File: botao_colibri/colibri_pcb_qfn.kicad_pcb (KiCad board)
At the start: 2 copper layers, 72.5 x 47.1 mm, 39 parts, among them J1 USB4970-00-A_REVA, J2 TC2030, J3 Conn_01x02, J4 PJ-307C, SW1 B3F-3122, U1 ME54BS12, U4 NPM1300-QEAA-R7

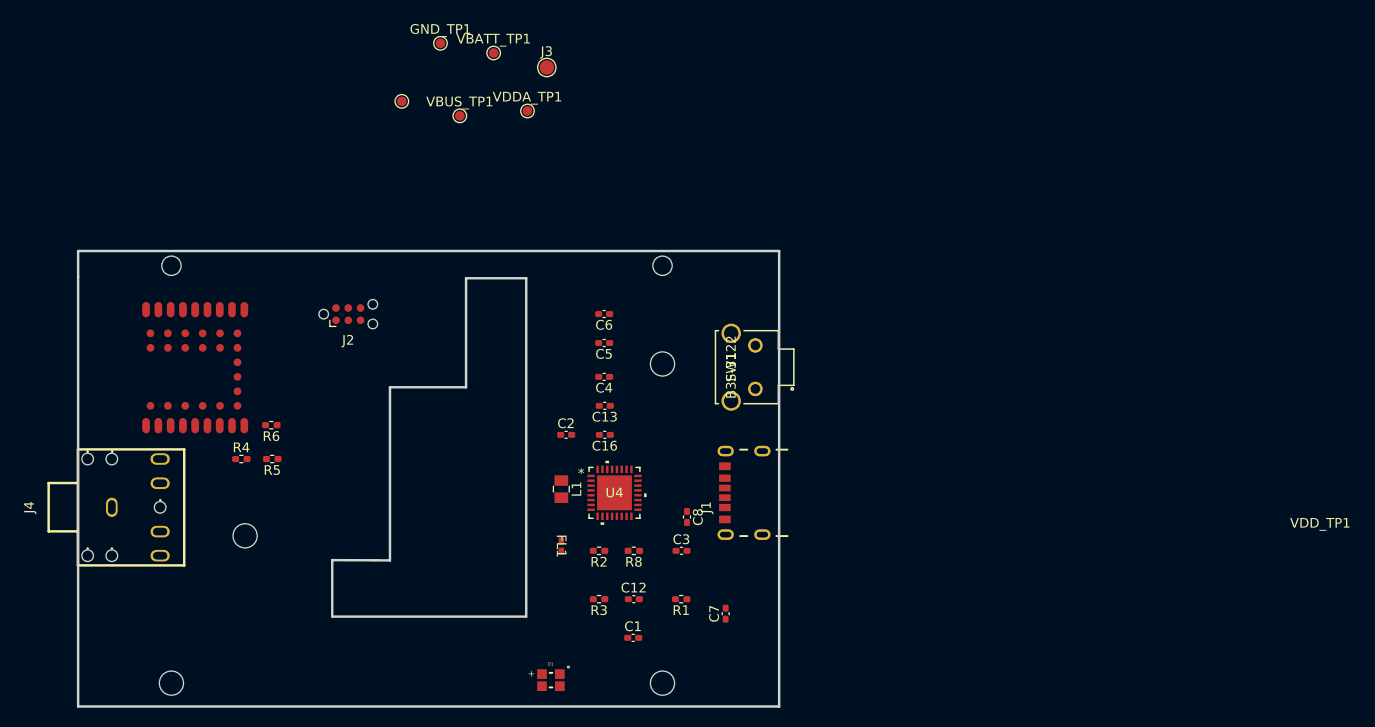
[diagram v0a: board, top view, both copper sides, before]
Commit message: mudanças de posição de componentes
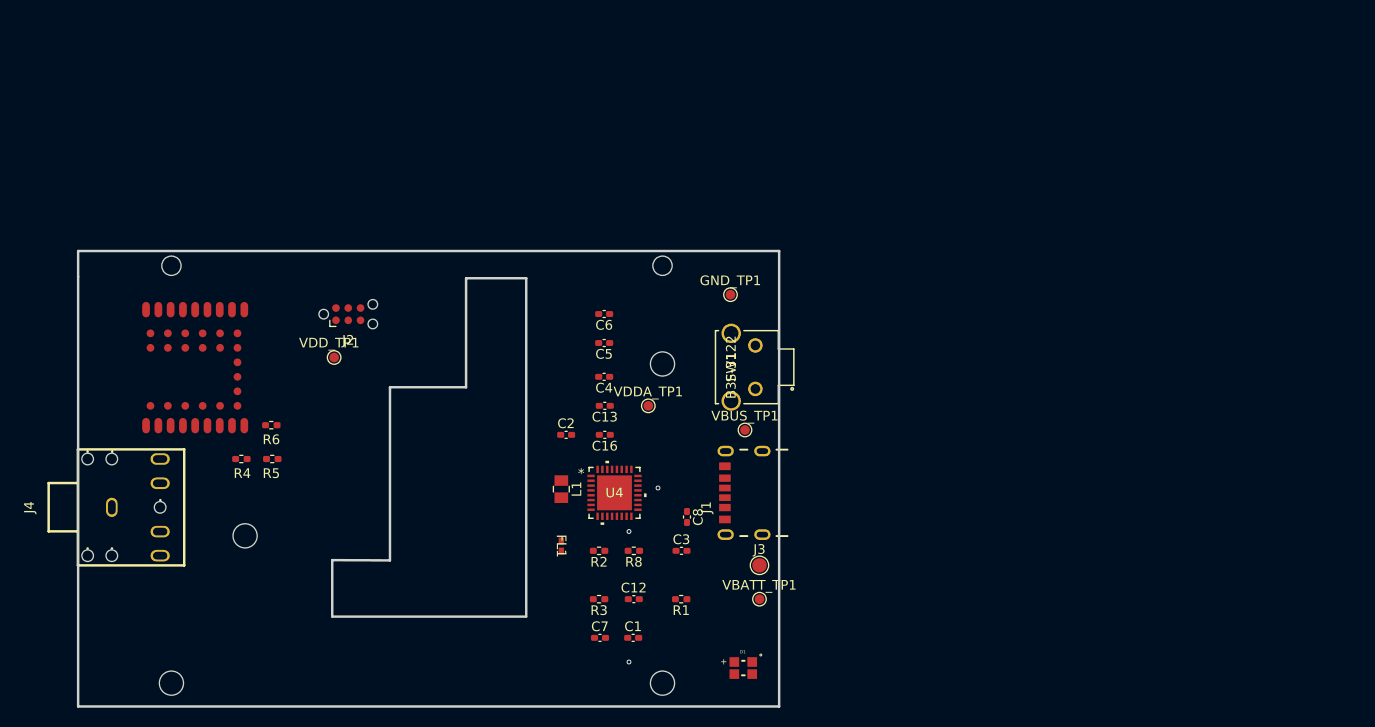
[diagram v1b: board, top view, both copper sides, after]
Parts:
- moved VBATT_TP1 62.8 mm to (194.5, 108.5)
- moved J3 56.0 mm to (194.5, 105.0)
- moved VBUS_TP1 43.9 mm to (193.0, 91.0)
- moved GND_TP1 39.7 mm to (191.5, 77.0)
- moved VDDA_TP1 33.0 mm to (183.0, 88.5)
- moved VDD_TP1 27.4 mm to (150.5, 83.5)
- moved D1 19.9 mm to (192.8, 115.6)
- moved C7 13.2 mm to (178.0, 112.5), turned to 0 degrees
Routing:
- net (no net): vias 0 -> 3
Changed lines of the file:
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@@
 	(footprint "colibri-v4:WL-SFCD_0805"
 		(layer "F.Cu")
-		(at 172.925 116.875)
+		(at 192.825 115.625)
 		(property "Reference" "D1"
 			(at -0.04 -1.6732 0)
@@
 	(footprint "TestPoint:TestPoint_Pad_D1.5mm"
 		(layer "F.Cu")
-		(at 172.5 53.5)
+		(at 194.5 105)
 		(descr "SMD pad as test Point, diameter 1.5mm")
 		(tags "test point SMD pad")
@@
 		(tags "resistor handsolder")
 		(property "Reference" "R4"
-			(at 0 -1.17 0)
+			(at 0.0975 1.5 0)
 			(layer "F.SilkS")
 			(effects
@@
 		(tags "resistor handsolder")
 		(property "Reference" "R6"
-			(at 0 -1.17 0)
+			(at 0 -1.5 0)
 			(layer "F.SilkS")
 			(effects
@@
 	(footprint "TestPoint:TestPoint_Pad_D1.0mm"
 		(layer "F.Cu")
-		(at 161.5 51)
+		(at 191.5 77)
 		(descr "SMD pad as test Point, diameter 1.0mm")
 		(tags "test point SMD pad")
@@
 	(footprint "Capacitor_SMD:C_0402_1005Metric_Pad0.74x0.62mm_HandSolder"
 		(layer "F.Cu")
-		(at 191 110 90)
+		(at 178 112.5)
 		(descr "Capacitor SMD 0402 (1005 Metric), square (rectangular) end terminal, IPC-7351 nominal with elongated pad for handsoldering. (Body size source: IPC-SM-782 page 76, https://www.pcb-3d.com/wordpress/wp-content/uploads/ipc-sm-782a_amendment_1_and_2.pdf)")
 		(tags "capacitor handsolder")
 		(property "Reference" "C7"
-			(at 0 -1.16 90)
+			(at 0 -1.16 0)
 			(layer "F.SilkS")
 			(effects
@@
 		)
 		(property "Value" "C_Small"
-			(at 0 1.16 90)
+			(at 0 1.16 0)
 			(layer "F.Fab")
 			(effects
@@
 		)
 		(property "Datasheet" ""
-			(at 0 0 90)
+			(at 0 0 0)
 			(layer "F.Fab")
 			(hide yes)
@@
 		)
 		(property "Description" "Unpolarized capacitor, small symbol"
-			(at 0 0 90)
+			(at 0 0 0)
 			(layer "F.Fab")
 			(hide yes)
@@
 		)
 		(property "KiLib_Generator" "SMD_2terminal_chip_molded"
-			(at 0 0 90)
+			(at 0 0 0)
 			(layer "F.SilkS")
 			(hide yes)
@@
 		)
 		(fp_text user "${REFERENCE}"
-			(at 0 0 90)
+			(at 0 0 0)
 			(layer "F.Fab")
 			(effects
@@
 		)
 		(pad "1" smd roundrect
-			(at -0.5675 0 90)
+			(at -0.5675 0)
 			(size 0.735 0.62)
 			(layers "F.Cu" "F.Mask" "F.Paste")
@@
 		)
 		(pad "2" smd roundrect
-			(at 0.5675 0 90)
+			(at 0.5675 0)
 			(size 0.735 0.62)
 			(layers "F.Cu" "F.Mask" "F.Paste")
@@
 	(footprint "TestPoint:TestPoint_Pad_D1.0mm"
 		(layer "F.Cu")
-		(at 167 52)
+		(at 194.5 108.5)
 		(descr "SMD pad as test Point, diameter 1.0mm")
 		(tags "test point SMD pad")
@@
 	(footprint "TestPoint:TestPoint_Pad_D1.0mm"
 		(layer "F.Cu")
-		(at 170.5 58)
+		(at 183 88.5)
 		(descr "SMD pad as test Point, diameter 1.0mm")
 		(tags "test point SMD pad")
@@
 	(footprint "TestPoint:TestPoint_Pad_D1.0mm"
 		(layer "F.Cu")
-		(at 163.5 58.5)
+		(at 193 91)
 		(descr "SMD pad as test Point, diameter 1.0mm")
 		(tags "test point SMD pad")
@@
 	(footprint "TestPoint:TestPoint_Pad_D1.0mm"
 		(layer "F.Cu")
-		(at 157.5 57)
+		(at 150.5 83.5)
 		(descr "SMD pad as test Point, diameter 1.0mm")
 		(tags "test point SMD pad")
 		(property "Reference" "VDD_TP1"
-			(at 95.0175 43.637 0)
+			(at -0.5 -1.5 0)
 			(layer "F.SilkS")
 			(effects
@@
 		)
 		(fp_text user "${REFERENCE}"
-			(at 95.0175 43.635 0)
+			(at -0.5 -1.502 0)
 			(layer "F.Fab")
 			(effects
@@
 		(tags "resistor handsolder")
 		(property "Reference" "R5"
-			(at 0 -1.17 0)
+			(at 0.0975 -1.5 0)
 			(layer "F.SilkS")
 			(effects
@@
 		(net "")
 	)
+	(via
+		(at 184 97)
+		(size 0.5)
+		(drill 0.3)
+		(layers "F.Cu" "B.Cu")
+		(net "")
+	)
+	(via
+		(at 181 101.5)
+		(size 0.5)
+		(drill 0.3)
+		(layers "F.Cu" "B.Cu")
+		(net "")
+	)
+	(via
+		(at 181 115)
+		(size 0.5)
+		(drill 0.3)
+		(layers "F.Cu" "B.Cu")
+		(net "")
+	)

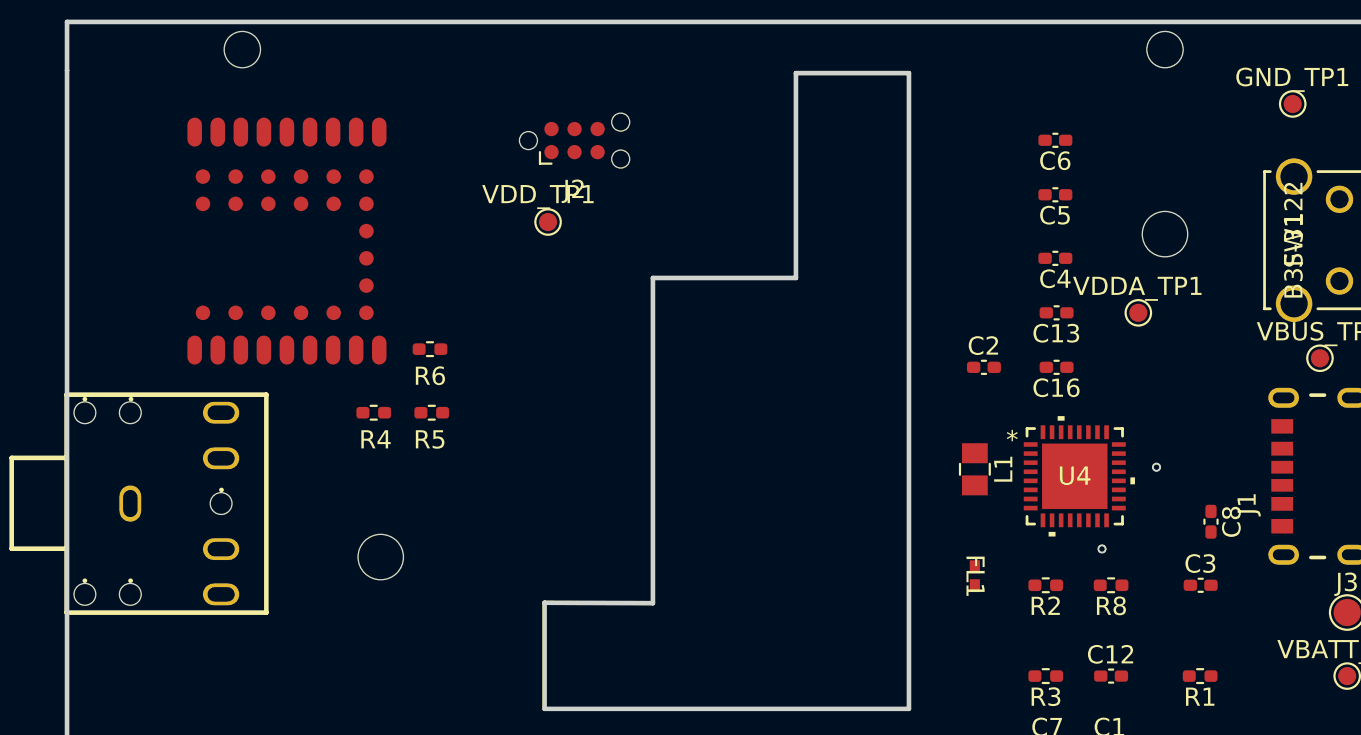
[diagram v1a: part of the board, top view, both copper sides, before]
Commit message: Desenho do silk do microcontrolador
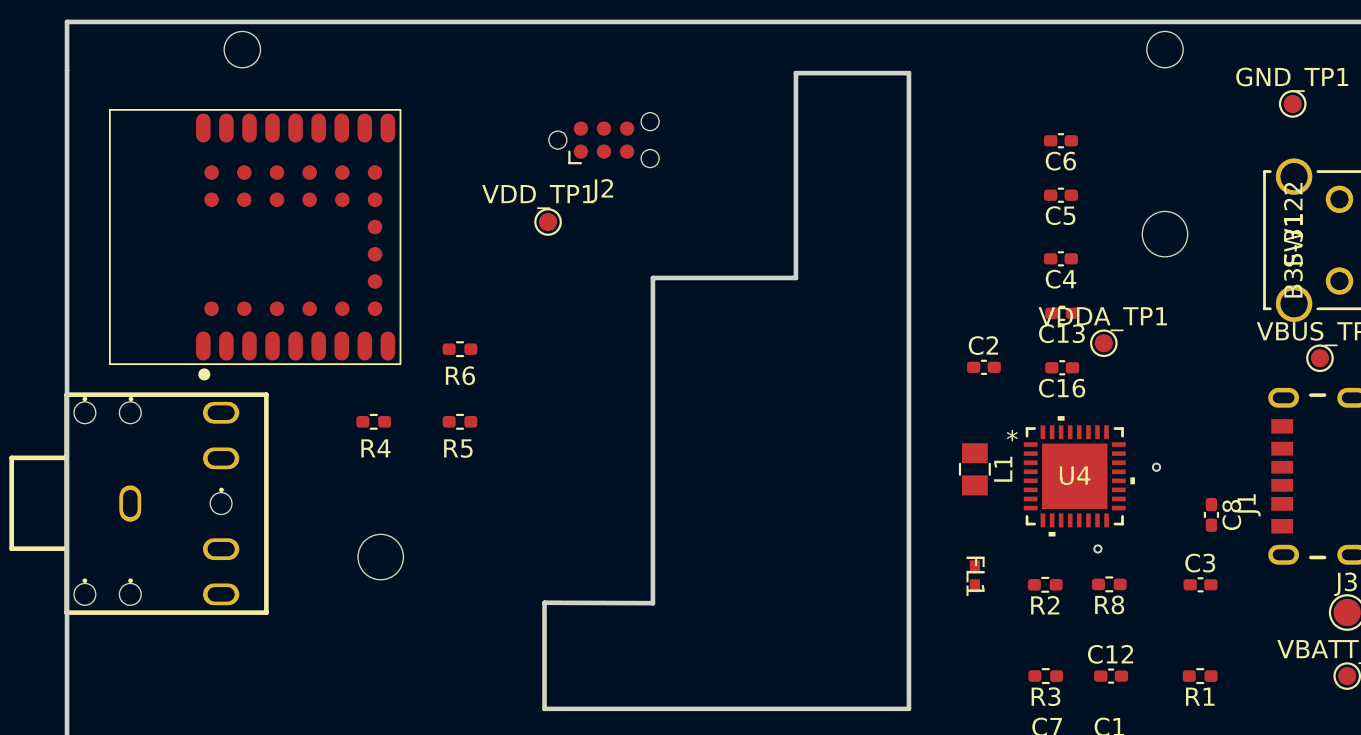
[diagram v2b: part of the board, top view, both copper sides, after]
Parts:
- moved VDDA_TP1 2.53 mm to (181.1, 90.2)
- moved R6 1.65 mm to (145.7, 90.5)
- moved R5 1.63 mm to (145.7, 94.5)
- moved J2 1.62 mm to (153.6, 79.0)
- moved U1 0.53 mm to (142.4, 90.3)
- moved R4 0.50 mm to (140.9, 94.5)
- moved C8 0.38 mm to (187.0, 99.6)
- moved C13 0.31 mm to (178.8, 88.5)
- moved C16 0.31 mm to (178.8, 91.5)
- moved C4 0.31 mm to (178.7, 85.5)
- moved C5 0.31 mm to (178.7, 82.0)
- moved C6 0.31 mm to (178.7, 79.0)
- moved R8 0.11 mm to (181.4, 103.5)
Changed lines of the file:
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@@
 	(footprint "Capacitor_SMD:C_0402_1005Metric_Pad0.74x0.62mm_HandSolder"
 		(layer "F.Cu")
-		(at 178.4325 79 180)
+		(at 178.74 79.025 180)
 		(descr "Capacitor SMD 0402 (1005 Metric), square (rectangular) end terminal, IPC-7351 nominal with elongated pad for handsoldering. (Body size source: IPC-SM-782 page 76, https://www.pcb-3d.com/wordpress/wp-content/uploads/ipc-sm-782a_amendment_1_and_2.pdf)")
 		(tags "capacitor handsolder")
@@
 	(footprint "Connector:Tag-Connect_TC2030-IDC-NL_2x03_P1.27mm_Vertical"
 		(layer "F.Cu")
-		(at 151.96 79.016)
+		(at 153.58 78.99)
 		(descr "Tag-Connect programming header; http://www.tag-connect.com/Materials/TC2030-IDC-NL.pdf")
 		(tags "tag connect programming header pogo pins")
@@
 			(polygon
 				(pts
-					(xy 153.23 78.381) (xy 150.69 78.381) (xy 150.69 79.651) (xy 153.23 79.651)
+					(xy 154.85 78.355) (xy 152.31 78.355) (xy 152.31 79.625) (xy 154.85 79.625)
 				)
 			)
@@
 	(footprint "Capacitor_SMD:C_0402_1005Metric_Pad0.74x0.62mm_HandSolder"
 		(layer "F.Cu")
-		(at 186.4325 103.5)
+		(at 186.425 103.475)
 		(descr "Capacitor SMD 0402 (1005 Metric), square (rectangular) end terminal, IPC-7351 nominal with elongated pad for handsoldering. (Body size source: IPC-SM-782 page 76, https://www.pcb-3d.com/wordpress/wp-content/uploads/ipc-sm-782a_amendment_1_and_2.pdf)")
 		(tags "capacitor handsolder")
@@
 	(footprint "Resistor_SMD:R_0402_1005Metric_Pad0.72x0.64mm_HandSolder"
 		(layer "F.Cu")
-		(at 140.9025 94)
+		(at 140.9025 94.5)
 		(descr "Resistor SMD 0402 (1005 Metric), square (rectangular) end terminal, IPC-7351 nominal with elongated pad for handsoldering. (Body size source: IPC-SM-782 page 72, https://www.pcb-3d.com/wordpress/wp-content/uploads/ipc-sm-782a_amendment_1_and_2.pdf)")
 		(tags "resistor handsolder")
@@
 	(footprint "Capacitor_SMD:C_0402_1005Metric_Pad0.74x0.62mm_HandSolder"
 		(layer "F.Cu")
-		(at 187 100 -90)
+		(at 187.025 99.625 -90)
 		(descr "Capacitor SMD 0402 (1005 Metric), square (rectangular) end terminal, IPC-7351 nominal with elongated pad for handsoldering. (Body size source: IPC-SM-782 page 76, https://www.pcb-3d.com/wordpress/wp-content/uploads/ipc-sm-782a_amendment_1_and_2.pdf)")
 		(tags "capacitor handsolder")
@@
 	(footprint "Resistor_SMD:R_0402_1005Metric_Pad0.72x0.64mm_HandSolder"
 		(layer "F.Cu")
-		(at 144 90.5 180)
+		(at 145.6525 90.5 180)
 		(descr "Resistor SMD 0402 (1005 Metric), square (rectangular) end terminal, IPC-7351 nominal with elongated pad for handsoldering. (Body size source: IPC-SM-782 page 72, https://www.pcb-3d.com/wordpress/wp-content/uploads/ipc-sm-782a_amendment_1_and_2.pdf)")
 		(tags "resistor handsolder")
@@
 	(footprint "Resistor_SMD:R_0402_1005Metric_Pad0.72x0.64mm_HandSolder"
 		(layer "F.Cu")
-		(at 181.5 103.5 180)
+		(at 181.4 103.45 180)
 		(descr "Resistor SMD 0402 (1005 Metric), square (rectangular) end terminal, IPC-7351 nominal with elongated pad for handsoldering. (Body size source: IPC-SM-782 page 72, https://www.pcb-3d.com/wordpress/wp-content/uploads/ipc-sm-782a_amendment_1_and_2.pdf)")
 		(tags "resistor handsolder")
@@
 	(footprint "Capacitor_SMD:C_0402_1005Metric_Pad0.74x0.62mm_HandSolder"
 		(layer "F.Cu")
-		(at 178.4325 85.5 180)
+		(at 178.74 85.525 180)
 		(descr "Capacitor SMD 0402 (1005 Metric), square (rectangular) end terminal, IPC-7351 nominal with elongated pad for handsoldering. (Body size source: IPC-SM-782 page 76, https://www.pcb-3d.com/wordpress/wp-content/uploads/ipc-sm-782a_amendment_1_and_2.pdf)")
 		(tags "capacitor handsolder")
@@
 	(footprint "Resistor_SMD:R_0402_1005Metric_Pad0.72x0.64mm_HandSolder"
 		(layer "F.Cu")
-		(at 177.9025 103.5 180)
+		(at 177.875 103.475 180)
 		(descr "Resistor SMD 0402 (1005 Metric), square (rectangular) end terminal, IPC-7351 nominal with elongated pad for handsoldering. (Body size source: IPC-SM-782 page 72, https://www.pcb-3d.com/wordpress/wp-content/uploads/ipc-sm-782a_amendment_1_and_2.pdf)")
 		(tags "resistor handsolder")
@@
 	(footprint "Capacitor_SMD:C_0402_1005Metric_Pad0.74x0.62mm_HandSolder"
 		(layer "F.Cu")
-		(at 178.4325 82 180)
+		(at 178.74 82.025 180)
 		(descr "Capacitor SMD 0402 (1005 Metric), square (rectangular) end terminal, IPC-7351 nominal with elongated pad for handsoldering. (Body size source: IPC-SM-782 page 76, https://www.pcb-3d.com/wordpress/wp-content/uploads/ipc-sm-782a_amendment_1_and_2.pdf)")
 		(tags "capacitor handsolder")
@@
 	(footprint "Capacitor_SMD:C_0402_1005Metric_Pad0.74x0.62mm_HandSolder"
 		(layer "F.Cu")
-		(at 178.5 91.5 180)
+		(at 178.8075 91.525 180)
 		(descr "Capacitor SMD 0402 (1005 Metric), square (rectangular) end terminal, IPC-7351 nominal with elongated pad for handsoldering. (Body size source: IPC-SM-782 page 76, https://www.pcb-3d.com/wordpress/wp-content/uploads/ipc-sm-782a_amendment_1_and_2.pdf)")
 		(tags "capacitor handsolder")
@@
 	(footprint "TestPoint:TestPoint_Pad_D1.0mm"
 		(layer "F.Cu")
-		(at 183 88.5)
+		(at 181.1 90.175)
 		(descr "SMD pad as test Point, diameter 1.0mm")
 		(tags "test point SMD pad")
@@
 	(footprint "Resistor_SMD:R_0402_1005Metric_Pad0.72x0.64mm_HandSolder"
 		(layer "F.Cu")
-		(at 144.0975 94 180)
+		(at 145.6525 94.5 180)
 		(descr "Resistor SMD 0402 (1005 Metric), square (rectangular) end terminal, IPC-7351 nominal with elongated pad for handsoldering. (Body size source: IPC-SM-782 page 72, https://www.pcb-3d.com/wordpress/wp-content/uploads/ipc-sm-782a_amendment_1_and_2.pdf)")
 		(tags "resistor handsolder")
@@
 	(footprint "Capacitor_SMD:C_0402_1005Metric_Pad0.74x0.62mm_HandSolder"
 		(layer "F.Cu")
-		(at 178.5 88.5 180)
+		(at 178.8075 88.525 180)
 		(descr "Capacitor SMD 0402 (1005 Metric), square (rectangular) end terminal, IPC-7351 nominal with elongated pad for handsoldering. (Body size source: IPC-SM-782 page 76, https://www.pcb-3d.com/wordpress/wp-content/uploads/ipc-sm-782a_amendment_1_and_2.pdf)")
 		(tags "capacitor handsolder")
@@
 	(footprint "colibri-v4:ME54BS12_V1.0"
 		(layer "F.Cu")
-		(at 141.9 90.55 90)
+		(at 142.375 90.325714 90)
 		(property "Reference" "U1"
 			(at 4.7546 -18.1292 90)
@@
 		(sheetname "/botao_mcu/")
 		(sheetfile "colibri_pcb_qfn.kicad_sch")
-		(units
-			(unit
-				(name "A")
-				(pins "1" "2" "3" "4" "5" "6" "7" "8" "9" "B1" "C1" "D1" "E1" "F1" "F2"
-					"C5" "B5" "A5" "A1" "10" "11" "18" "17" "16" "15" "14" "13" "12" "A6"
-					"B6" "C6" "D5" "D6" "E5" "E6" "F3" "F4" "F5" "F6"
-				)
+		(duplicate_pad_numbers_are_jumpers no)
+		(fp_rect
+			(start -1 -16)
+			(end 13 0)
+			(stroke
+				(width 0.1)
+				(type default)
 			)
+			(fill no)
+			(layer "F.SilkS")
 		)
-		(duplicate_pad_numbers_are_jumpers no)
 		(fp_circle
-			(center -1.16642 -10.795)
-			(end -1.16642 -10.795)
+			(center -1.56573 -10.8)
+			(end -1.76573 -11)
 			(stroke
 				(width 0.1)
 				(type solid)
 			)
-			(fill no)
+			(fill yes)
 			(layer "F.SilkS")
 		)
@@
 	)
 	(via
-		(at 181 101.5)
+		(at 180.775 101.5)
 		(size 0.5)
 		(drill 0.3)
